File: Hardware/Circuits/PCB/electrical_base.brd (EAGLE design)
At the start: 56 x 164 mm, 13 parts, among them Q1 XT60_YELLOW, Q2 XT60_YELLOW, X1 B2P-VH, X2 B2P-VH, X3 B2P-VH, X4 B2P-VH

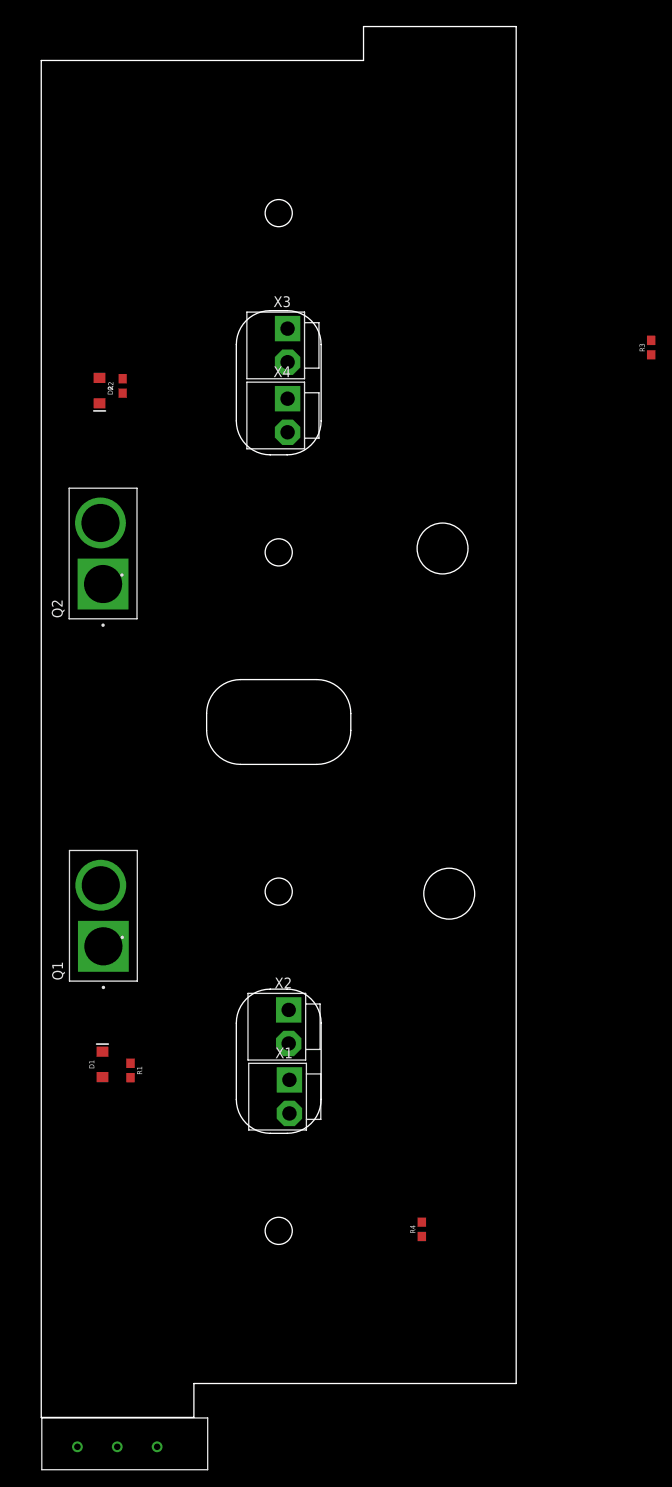
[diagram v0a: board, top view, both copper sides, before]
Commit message: enable Motor
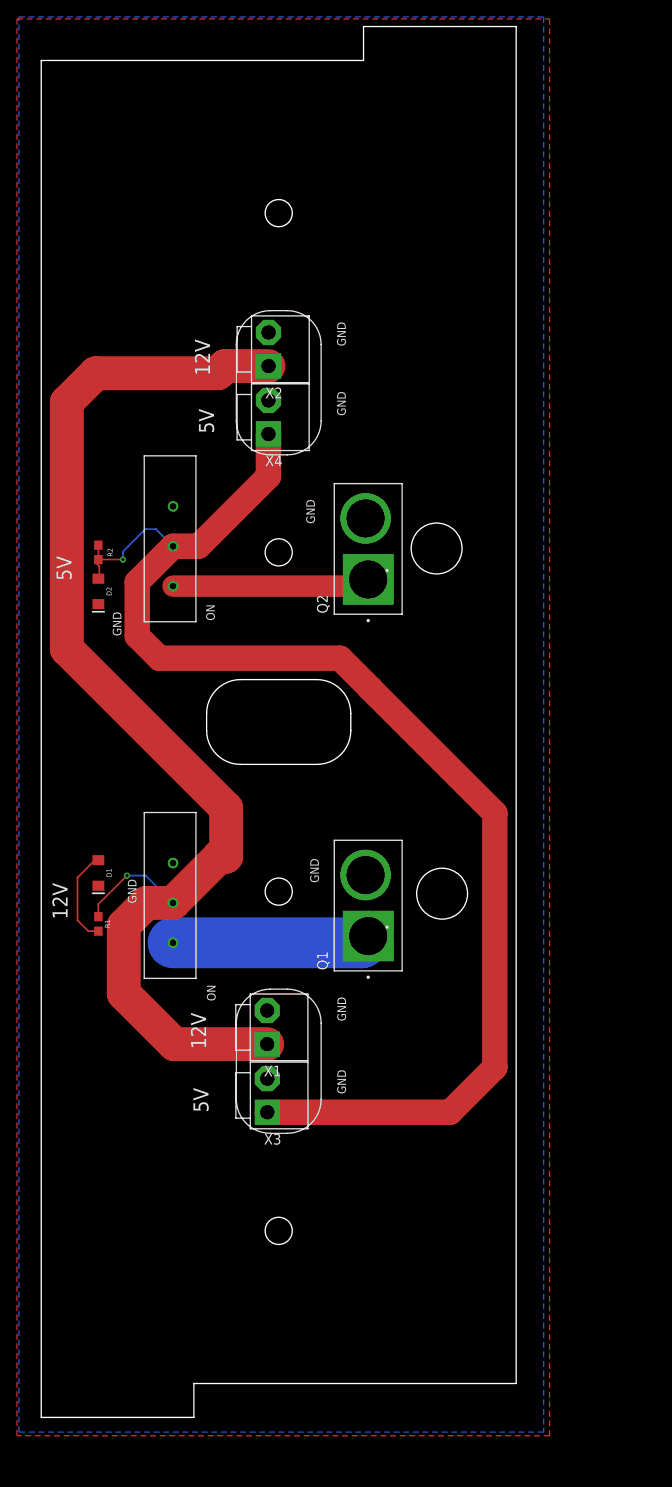
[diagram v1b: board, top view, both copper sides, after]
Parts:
- removed R3, R4: 1k, SparkFun-Resistors:0603
- added U$2: SWITCH_3P_4.7, switch_3p_4.7mm:3P
- moved X3 88.5 mm to (26.8, 38.1), turned to 90 degrees
- moved X2 79.9 mm to (27.0, 126.1), turned to 90 degrees
- moved U$1 62.0 mm to (15.8, 57.8), turned to 90 degrees
- moved Q2 31.3 mm to (38.7, 102.6)
- moved Q1 31.2 mm to (38.7, 60.5)
- moved D2 23.7 mm to (6.89, 97.5)
- moved D1 22.6 mm to (6.89, 64.3), turned to 270 degrees
- moved R2 19.8 mm to (6.89, 102.1), turned to 270 degrees
- moved R1 17.7 mm to (6.89, 58.3)
- moved X1 8.58 mm to (26.8, 46.1), turned to 90 degrees
- moved X4 2.26 mm to (26.9, 118.1), turned to 90 degrees
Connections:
- removed net N$1: R4.1
- removed net N$2: R4.2
- removed net N$3: R3.1
- removed net N$4: R3.2
- new net 5V_S: R2.1, U$2.P$2, X3.1, X4.1
- new net N$7: U$2.P$3
- net 5V: now also U$2.P$1; no longer R2.1, X3.1, X4.1
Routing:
- net 5V_S: track 0.00 -> 155.2 mm, vias 0 -> 1
- net 12V_S: track 0.00 -> 143.2 mm, vias 0 -> 1
- net 12V: track 0.00 -> 23.3 mm
- net 5V: track 0.00 -> 23.3 mm
- net N$9: track 0.00 -> 11.3 mm
- net N$10: track 0.00 -> 2.66 mm
- added copper zone on layer 1, net GND
- added copper zone on layer 16, net GND
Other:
- outline, holes or cut-outs redrawn
- board text added: "12V"
- board text added: "5V"
- board text added: "GND"
- board text added: "ON"

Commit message: update circuits
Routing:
- net 5V_S: track 155.2 -> 154.5 mm
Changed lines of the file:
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@@
 <setting verticaltext="up"/>
 </settings>
-<grid distance="1" unitdist="mic" unit="mm" style="lines" multiple="1" display="no" altdistance="5" altunitdist="mil" altunit="mm"/>
+<grid distance="0.0393700787" unitdist="mil" unit="mil" style="lines" multiple="1" display="no" altdistance="5" altunitdist="mil" altunit="mil"/>
 <layers>
 <layer number="1" name="Top" color="4" fill="1" visible="yes" active="yes"/>
@@
 <contactref element="Q2" pad="2"/>
 <contactref element="Q1" pad="2"/>
-<polygon width="0.2032" layer="1">
+<polygon width="0.2032" layer="1" isolate="0.00508125">
 <vertex x="-2.706" y="165.044"/>
 <vertex x="60.092" y="165.044"/>
@@
 <vertex x="-2.706" y="-2.008"/>
 </polygon>
-<polygon width="0.2032" layer="16">
+<polygon width="0.2032" layer="16" isolate="0.00508125">
 <vertex x="-2.473" y="165.277"/>
 <vertex x="59.394" y="165.277"/>
@@
 <contactref element="R1" pad="2"/>
 <contactref element="D1" pad="A"/>
-<wire x1="6.894" y1="57.488" x2="5.71" y2="57.488" width="0.2032" layer="1"/>
-<wire x1="5.71" y1="57.488" x2="4.432" y2="58.766" width="0.2032" layer="1"/>
-<wire x1="4.432" y1="58.766" x2="4.432" y2="63.803" width="0.2032" layer="1"/>
 <wire x1="6.477" y1="65.848" x2="6.894" y2="65.848" width="0.2032" layer="1"/>
-<wire x1="4.432" y1="63.803" x2="6.477" y2="65.848" width="0.2032" layer="1"/>
+<wire x1="6.307" y1="65.678" x2="6.477" y2="65.848" width="0.2032" layer="1"/>
+<wire x1="5.71" y1="57.488" x2="4.432" y2="58.766" width="0.4064" layer="1"/>
+<wire x1="6.894" y1="57.488" x2="5.71" y2="57.488" width="0.4064" layer="1"/>
+<wire x1="4.432" y1="58.766" x2="4.432" y2="63.803" width="0.4064" layer="1"/>
+<wire x1="4.432" y1="63.803" x2="6.307" y2="65.678" width="0.4064" layer="1"/>
 </signal>
 <signal name="N$10">
 <contactref element="R2" pad="2"/>
 <contactref element="D2" pad="A"/>
-<wire x1="7" y1="100.5" x2="6.5" y2="101" width="0.2032" layer="1"/>
-<wire x1="7" y1="99.5" x2="7" y2="100.5" width="0.2032" layer="1"/>
-<wire x1="6.5" y1="101" x2="6.894" y2="101.292" width="0.2032" layer="1"/>
-<wire x1="7" y1="99.5" x2="6.894" y2="99.045" width="0.2032" layer="1"/>
+<wire x1="6.79925625" y1="101.221784375" x2="6.845084375" y2="101.25575" width="0.2032" layer="1"/>
+<wire x1="6.845084375" y1="101.25575" x2="6.894" y2="101.292" width="0.2032" layer="1"/>
+<wire x1="6.894" y1="99.045" x2="6.894" y2="100.66329375" width="0.4064" layer="1"/>
+<wire x1="6.894" y1="100.66329375" x2="6.56861875" y2="100.988675" width="0.4064" layer="1"/>
+<wire x1="6.56861875" y1="100.988675" x2="6.57479375" y2="100.982565625" width="0.4064" layer="1"/>
+<wire x1="6.884228125" y1="101.292" x2="6.894" y2="101.292" width="0.4064" layer="1"/>
+<wire x1="6.57479375" y1="100.982565625" x2="6.884228125" y2="101.292" width="0.4064" layer="1"/>
 </signal>
 <signal name="5V">
@@
 <wire x1="21.965" y1="71.971" x2="21.965" y2="67.078" width="4" layer="1"/>
 <wire x1="21.965" y1="67.078" x2="21.196" y2="66.309" width="4" layer="1"/>
-<wire x1="15.7" y1="60.813" x2="12.477" y2="64.036" width="0.2032" layer="16"/>
+<wire x1="12.477" y1="64.036" x2="12.565" y2="63.948" width="0.2032" layer="16"/>
 <via x="10.264" y="64.036" extent="1-16" drill="0.35"/>
-<wire x1="10.264" y1="64.036" x2="6.894" y2="60.666" width="0.2032" layer="1"/>
-<wire x1="6.894" y1="60.666" x2="6.894" y2="59.188" width="0.2032" layer="1"/>
-<wire x1="12.477" y1="64.036" x2="10.264" y2="64.036" width="0.2032" layer="16"/>
+<wire x1="15.6335" y1="60.8795" x2="15.7" y2="60.813" width="0.2032" layer="16"/>
+<wire x1="6.931" y1="60.703" x2="7.0375" y2="60.8095" width="0.2032" layer="1"/>
+<wire x1="6.894" y1="59.188" x2="6.894" y2="60.666" width="0.4064" layer="1"/>
+<wire x1="6.894" y1="60.666" x2="6.931" y2="60.703" width="0.4064" layer="1"/>
+<wire x1="7.0375" y1="60.8095" x2="10.264" y2="64.036" width="0.4064" layer="1"/>
+<wire x1="10.264" y1="64.036" x2="12.477" y2="64.036" width="0.4064" layer="16"/>
+<wire x1="12.565" y1="63.948" x2="15.6335" y2="60.8795" width="0.4064" layer="16"/>
 </signal>
 <signal name="5V_S">
@@
 <wire x1="48.36" y1="36.132" x2="26.808" y2="36.132" width="3" layer="1"/>
 <wire x1="53.64138125" y1="41.41338125" x2="48.36" y2="36.132" width="3" layer="1"/>
-<wire x1="15.7" y1="102.8675" x2="13.6755" y2="104.892" width="0.2032" layer="16"/>
-<wire x1="9.798" y1="102.234" x2="9.798" y2="101.301" width="0.2032" layer="16"/>
 <via x="9.798" y="101.301" extent="1-16" drill="0.35"/>
-<wire x1="9.798" y1="101.301" x2="6.903" y2="101.301" width="0.2032" layer="1"/>
-<wire x1="6.903" y1="101.301" x2="6.894" y2="102.992" width="0.2032" layer="1"/>
-<wire x1="13.6755" y1="104.892" x2="12.456" y2="104.892" width="0.2032" layer="16"/>
-<wire x1="12.456" y1="104.892" x2="9.798" y2="102.234" width="0.2032" layer="16"/>
+<wire x1="9.798" y1="101.301" x2="9.7885" y2="101.2915" width="0.2032" layer="1"/>
+<wire x1="9.7885" y1="101.2915" x2="9.774" y2="101.277" width="0.2032" layer="1"/>
+<wire x1="12.456" y1="104.892" x2="12.586" y2="104.892" width="0.2032" layer="16"/>
+<wire x1="12.4025" y1="104.8385" x2="12.456" y2="104.892" width="0.2032" layer="16"/>
+<wire x1="9.798" y1="101.301" x2="10.82" y2="102.323" width="0.4064" layer="16"/>
+<wire x1="10.82" y1="103.256" x2="10.82" y2="102.323" width="0.4064" layer="16"/>
+<wire x1="10.82" y1="103.256" x2="12.4025" y2="104.8385" width="0.4064" layer="16"/>
+<wire x1="12.586" y1="104.892" x2="13.6755" y2="104.892" width="0.4064" layer="16"/>
+<wire x1="13.6755" y1="104.892" x2="15.7" y2="102.8675" width="0.4064" layer="16"/>
+<wire x1="6.894" y1="102.992" x2="8.563" y2="102.992" width="0.4064" layer="1"/>
+<wire x1="9.7885" y1="101.7665" x2="9.7885" y2="101.2915" width="0.4064" layer="1"/>
+<wire x1="8.563" y1="102.992" x2="9.7885" y2="101.7665" width="0.4064" layer="1"/>
 </signal>
 <signal name="N$7">
